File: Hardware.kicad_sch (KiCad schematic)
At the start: 29 parts, among them J1 Conn_01x06_Socket, J5 Conn_01x05_Socket, Q1 BC849, Q2 BC849, SW1 Push_Button, SW2 Push_Button, U1 ESP32-WROOM-32, U9 AMS1117-3.3

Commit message: done most of the schematics
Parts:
- removed C21, C24, C25, C26: C, symbol Device:C
- removed TP2: TestPoint, symbol Connector:TestPoint
- removed U9: AMS1117-3.3, Package_TO_SOT_SMD:SOT-223-3_TabPin2, symbol Regulator_Linear:AMS1117-3.3
- added C2, C3, C8, C9: C, symbol Device:C
- added TP6: TestPoint, symbol Connector:TestPoint
- added U7: AMS1117-3.3, Package_TO_SOT_SMD:SOT-223-3_TabPin2, symbol Regulator_Linear:AMS1117-3.3
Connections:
- net +5V: now also C2.1, C3.1, U7.3 (VI)
- net GND: now also C2.2, C3.2, C8.2, C9.2, TP6.1, U7.1 (GND)
- net GPS_RX: no longer U1.28 (IO17)
- net GPS_TX: no longer U1.33 (IO21)
- net LTE_RX: no longer U1.16 (IO13)
- net LTE_TX: no longer U1.27 (IO16)
- net SD_CS: no longer U1.36 (IO22)
- net ANT_CTRL: no longer names the net of U1.11 (IO26)
- net PSU_MCU renamed PSU
- net PSU: now also C8.1, C9.1, U7.2 (VO)
- net PWRKEY: no longer names the net of U1.10 (IO25)
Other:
- note added: "PSU"

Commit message: done refacoring
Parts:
- C2, C8: value C -> 10uF
- C3, C9: value C -> 100pF
- H1, H2, H3, H4: footprint (none) -> MountingHole:MountingHole_3.2mm_M3_DIN965_Pad
- J5: footprint (none) -> Connector_PinHeader_1.00mm:PinHeader_1x05_P1.00mm_Vertical
- R1, R3, R4: footprint Resistor_SMD:R_1206_3216Metric_Pad1.30x1.75mm_HandSolder -> (none)
- TP13, TP14, TP15, TP16, TP6: footprint (none) -> TestPoint:TestPoint_Pad_D2.5mm

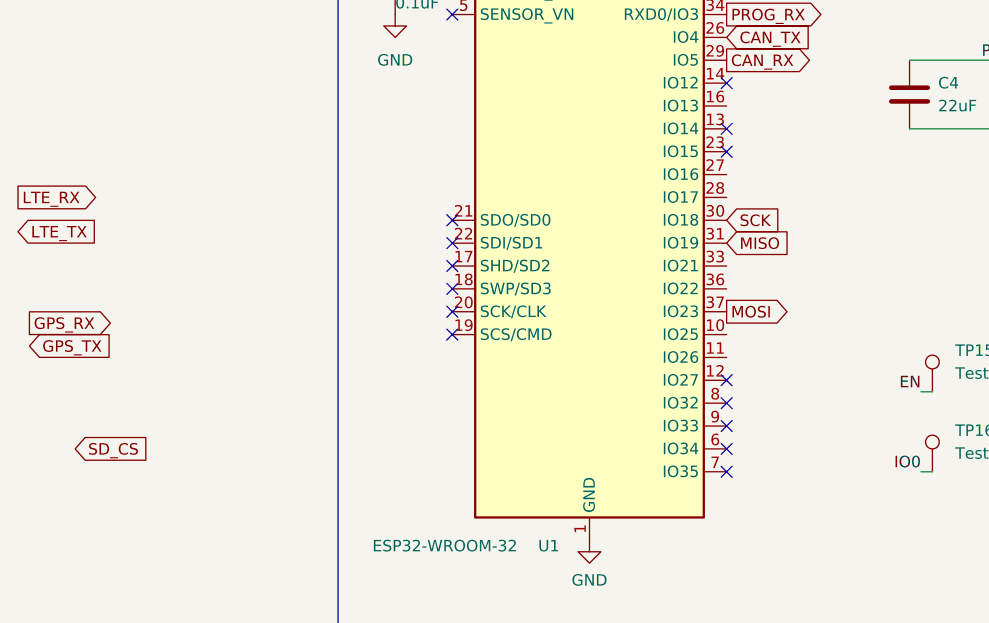
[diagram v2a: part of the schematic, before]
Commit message: assigned most footprints
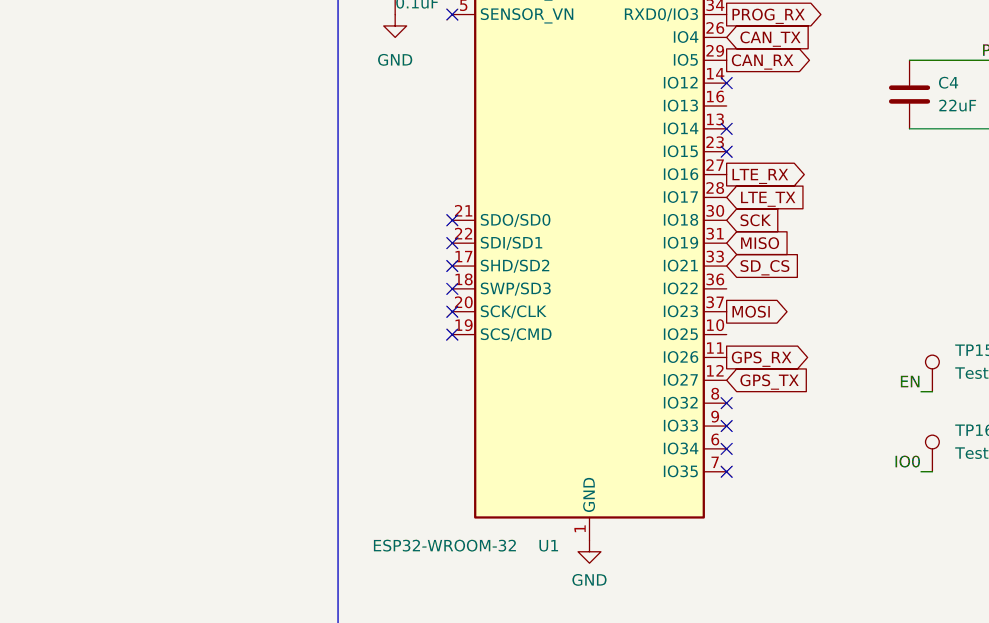
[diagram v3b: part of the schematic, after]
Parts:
- C1, C22, C23, C5: footprint Capacitor_SMD:C_0805_2012Metric_Pad1.18x1.45mm_HandSolder -> (none)
- C4: footprint Capacitor_SMD:C_1206_3216Metric_Pad1.33x1.80mm_HandSolder -> (none)
- R1, R3, R4: footprint (none) -> Resistor_SMD:R_0603_1608Metric
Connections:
- net GPS_RX: now also U1.11 (IO26)
- net GPS_TX: now also U1.12 (IO27)
- net LTE_RX: now also U1.27 (IO16)
- net LTE_TX: now also U1.28 (IO17)
- net SD_CS: now also U1.33 (IO21)
- no-connect marks 17 -> 16
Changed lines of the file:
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@@
 	)
 	(no_connect
-		(at 59.69 81.28)
-	)
-	(no_connect
 		(at 29.21 63.5)
 	)
@@
 	(global_label "LTE_RX"
 		(shape output)
-		(at -19.05 60.96 0)
+		(at 59.69 58.42 0)
 		(fields_autoplaced yes)
 		(effects
@@
 		)
 		(property "Intersheetrefs" "${INTERSHEET_REFS}"
-			(at -9.473 60.96 0)
+			(at 69.267 58.42 0)
 			(effects
 				(font
@@
 	(global_label "LTE_TX"
 		(shape input)
-		(at -19.05 64.77 0)
+		(at 59.69 60.96 0)
 		(fields_autoplaced yes)
 		(effects
@@
 		)
 		(property "Intersheetrefs" "${INTERSHEET_REFS}"
-			(at -9.7754 64.77 0)
+			(at 68.9646 60.96 0)
 			(effects
 				(font
@@
 	(global_label "GPS_RX"
 		(shape output)
-		(at -17.78 74.93 0)
+		(at 59.69 78.74 0)
 		(fields_autoplaced yes)
 		(effects
@@
 		)
 		(property "Intersheetrefs" "${INTERSHEET_REFS}"
-			(at -7.5982 74.93 0)
+			(at 69.8718 78.74 0)
 			(effects
 				(font
@@
 	(global_label "SD_CS"
 		(shape input)
-		(at -12.7 88.9 0)
+		(at 59.69 68.58 0)
 		(fields_autoplaced yes)
 		(effects
@@
 		)
 		(property "Intersheetrefs" "${INTERSHEET_REFS}"
-			(at -3.7882 88.9 0)
+			(at 68.6018 68.58 0)
 			(effects
 				(font
@@
 	(global_label "GPS_TX"
 		(shape input)
-		(at -17.78 77.47 0)
+		(at 59.69 81.28 0)
 		(fields_autoplaced yes)
 		(effects
@@
 		)
 		(property "Intersheetrefs" "${INTERSHEET_REFS}"
-			(at -7.9006 77.47 0)
+			(at 69.5694 81.28 0)
 			(effects
 				(font
@@
 			)
 		)
-		(property "Footprint" "Capacitor_SMD:C_0805_2012Metric_Pad1.18x1.45mm_HandSolder"
+		(property "Footprint" ""
 			(at 23.8252 40.64 0)
 			(effects
@@
 			)
 		)
-		(property "Footprint" ""
+		(property "Footprint" "Resistor_SMD:R_0603_1608Metric"
 			(at 166.37 84.328 90)
 			(effects
@@
 			)
 		)
-		(property "Footprint" ""
+		(property "Footprint" "Resistor_SMD:R_0603_1608Metric"
 			(at 166.37 72.898 90)
 			(effects
@@
 			)
 		)
-		(property "Footprint" ""
+		(property "Footprint" "Resistor_SMD:R_0603_1608Metric"
 			(at 21.082 29.21 90)
 			(effects
@@
 			)
 		)
-		(property "Footprint" "Capacitor_SMD:C_0805_2012Metric_Pad1.18x1.45mm_HandSolder"
+		(property "Footprint" ""
 			(at 120.65 28.2448 0)
 			(effects
@@
 			)
 		)
-		(property "Footprint" "Capacitor_SMD:C_0805_2012Metric_Pad1.18x1.45mm_HandSolder"
+		(property "Footprint" ""
 			(at 120.65 47.2948 0)
 			(effects
@@
 			)
 		)
-		(property "Footprint" "Capacitor_SMD:C_0805_2012Metric_Pad1.18x1.45mm_HandSolder"
+		(property "Footprint" ""
 			(at 92.4052 53.34 0)
 			(effects
@@
 			)
 		)
-		(property "Footprint" "Capacitor_SMD:C_1206_3216Metric_Pad1.33x1.80mm_HandSolder"
+		(property "Footprint" ""
 			(at 80.9752 53.34 0)
 			(effects

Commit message: cleaned up scematics and updated power management
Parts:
- C1, C22, C23, C3, C5, C9: footprint (none) -> Capacitor_SMD:C_0805_2012Metric
- C2, C8: footprint (none) -> Capacitor_SMD:C_1206_3216Metric
- C4: footprint (none) -> Capacitor_SMD:C_0603_1608Metric

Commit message: finelized scematics
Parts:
- removed SW1, SW2: Push_Button, Button_Switch_THT:SW_PUSH_6mm, symbol PCM_SL_Devices:Push_Button
- removed TP16: TestPoint, TestPoint:TestPoint_Pad_D2.5mm, symbol Connector:TestPoint
- added C42: 100pF, Capacitor_SMD:C_0805_2012Metric, symbol Device:C
- added D10: BZV55B5V1, Diode_SMD:D_MiniMELF, symbol Diode:BZV55B5V1
- added R22: 10K, Resistor_SMD:R_0603_1608Metric, symbol Device:R
- added R23: 3K9, Resistor_SMD:R_0603_1608Metric, symbol Device:R
- added SW1, SW3: SW_Push, Button_Switch_THT:SW_PUSH_6mm, symbol Switch:SW_Push
- added TP20, TP21: TestPoint, TestPoint:TestPoint_Pad_D2.0mm, symbol Connector:TestPoint
- J5: footprint Connector_PinHeader_1.00mm:PinHeader_1x05_P1.00mm_Vertical -> Connector_PinHeader_2.54mm:PinHeader_1x05_P2.54mm_Vertical
- TP13, TP14, TP15, TP6: footprint TestPoint:TestPoint_Pad_D2.5mm -> TestPoint:TestPoint_Pad_D2.0mm
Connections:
- net +3V3 is gone; now on net PSU: R1.1
- net PW- is gone; now on net GND: J5.2 (Pin_2)
- net ACC: now also R22.1
- net DTR: no longer J1.2 (Pin_2), Q1.2 (E), R4.1
- net EN: now also SW1.2, TP21.1; no longer TP15.1
- net GND: now also C42.2, D10.2 (A), R23.2, SW1.1, SW3.1
- net IO0: now also SW3.2, TP20.1
- net ACC_Readout: now reaches U1.8 (IO32)
- net ACC_Readout: now also TP15.1, C42.1, D10.1 (K), R22.2, R23.1
- new net RTS: J1.2 (Pin_2), Q1.2 (E), R4.1
- no-connect marks 16 -> 18
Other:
- note added: "ACC Readout"
- moved on the sheet: C2, C22, C23, C3, C8, C9, H1, H2, H3, H4, Q1, R3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

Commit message: mostly layouted
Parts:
- SW1, SW3: footprint Button_Switch_THT:SW_PUSH_6mm -> Jumper:SolderJumper-2_P1.3mm_Open_RoundedPad1.0x1.5mm
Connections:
- net GND: no longer TP6.1
- net PSU: now also TP6.1
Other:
- moved on the sheet: TP6
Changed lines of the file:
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@@
 		)
 	)
+	(wire
+		(pts
+			(xy 205.74 30.48) (xy 205.74 33.02)
+		)
+		(stroke
+			(width 0)
+			(type default)
+		)
+	)
 	(polyline
 		(pts
@@
 			)
 		)
-		(property "Footprint" "Button_Switch_THT:SW_PUSH_6mm"
+		(property "Footprint" "Jumper:SolderJumper-2_P1.3mm_Open_RoundedPad1.0x1.5mm"
 			(at 163.83 102.87 0)
 			(effects
@@
 	(symbol
 		(lib_id "Connector:TestPoint")
-		(at 205.74 40.64 180)
+		(at 205.74 30.48 0)
 		(unit 1)
 		(exclude_from_sim no)
@@
 		(fields_autoplaced yes)
 		(property "Reference" "TP6"
-			(at 208.28 42.6719 0)
+			(at 208.28 25.9079 0)
 			(effects
 				(font
 					(size 1.27 1.27)
 				)
-				(justify right)
+				(justify left)
 			)
 		)
 		(property "Value" "TestPoint"
-			(at 208.28 45.2119 0)
+			(at 208.28 28.4479 0)
 			(effects
 				(font
 					(size 1.27 1.27)
 				)
-				(justify right)
+				(justify left)
 			)
 		)
 		(property "Footprint" "TestPoint:TestPoint_Pad_D2.0mm"
-			(at 200.66 40.64 0)
+			(at 210.82 30.48 0)
 			(effects
 				(font
@@
 		)
 		(property "Datasheet" "~"
-			(at 200.66 40.64 0)
+			(at 210.82 30.48 0)
 			(effects
 				(font
@@
 		)
 		(property "Description" "test point"
-			(at 205.74 40.64 0)
+			(at 205.74 30.48 0)
 			(effects
 				(font
@@
 		)
 		(property "Availability" ""
-			(at 205.74 40.64 0)
+			(at 205.74 30.48 0)
 			(effects
 				(font
@@
 		)
 		(property "Check_prices" ""
-			(at 205.74 40.64 0)
+			(at 205.74 30.48 0)
 			(effects
 				(font
@@
 		)
 		(property "Description_1" ""
-			(at 205.74 40.64 0)
+			(at 205.74 30.48 0)
 			(effects
 				(font
@@
 		)
 		(property "MANUFACTURER" ""
-			(at 205.74 40.64 0)
+			(at 205.74 30.48 0)
 			(effects
 				(font
@@
 		)
 		(property "MAXIMUM_PACKAGE_HEIGHT" ""
-			(at 205.74 40.64 0)
+			(at 205.74 30.48 0)
 			(effects
 				(font
@@
 		)
 		(property "MF" ""
-			(at 205.74 40.64 0)
+			(at 205.74 30.48 0)
 			(effects
 				(font
@@
 		)
 		(property "MP" ""
-			(at 205.74 40.64 0)
+			(at 205.74 30.48 0)
 			(effects
 				(font
@@
 		)
 		(property "PARTREV" ""
-			(at 205.74 40.64 0)
+			(at 205.74 30.48 0)
 			(effects
 				(font
@@
 		)
 		(property "Package" ""
-			(at 205.74 40.64 0)
+			(at 205.74 30.48 0)
 			(effects
 				(font
@@
 		)
 		(property "Price" ""
-			(at 205.74 40.64 0)
+			(at 205.74 30.48 0)
 			(effects
 				(font
@@
 		)
 		(property "SNAPEDA_PN" ""
-			(at 205.74 40.64 0)
+			(at 205.74 30.48 0)
 			(effects
 				(font
@@
 		)
 		(property "STANDARD" ""
-			(at 205.74 40.64 0)
+			(at 205.74 30.48 0)
 			(effects
 				(font
@@
 		)
 		(property "SnapEDA_Link" ""
-			(at 205.74 40.64 0)
+			(at 205.74 30.48 0)
 			(effects
 				(font
@@
 			)
 		)
-		(property "Footprint" "Button_Switch_THT:SW_PUSH_6mm"
+		(property "Footprint" "Jumper:SolderJumper-2_P1.3mm_Open_RoundedPad1.0x1.5mm"
 			(at 193.04 102.87 0)
 			(effects

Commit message: pre remobing sd card
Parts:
- removed TP13, TP14, TP20, TP21: TestPoint, TestPoint:TestPoint_Pad_D2.0mm, symbol Connector:TestPoint
- TP15, TP6: footprint TestPoint:TestPoint_Pad_D2.0mm -> TestPoint:TestPoint_Pad_D1.5mm

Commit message: mostly finished layout
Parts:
- removed H3, H4: MountingHole_Pad, MountingHole:MountingHole_3.2mm_M3_DIN965_Pad, symbol Mechanical:MountingHole_Pad
- added H5, H6: MountingHole, MountingHole:MountingHole_3.2mm_M3, symbol Mechanical:MountingHole
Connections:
- net MISO: no longer names the net of U1.31 (IO19)
- net MOSI: no longer names the net of U1.37 (IO23)
- net SCK: no longer names the net of U1.30 (IO18)
- net SD_CS: no longer names the net of U1.33 (IO21)
- no-connect marks 18 -> 21
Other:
- removed sheet SD_Modula
